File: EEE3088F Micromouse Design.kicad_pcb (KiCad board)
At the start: 2 copper layers, 74.5 x 78.2 mm, 49 parts, among them J1 Conn_02x16_Odd_Even, J2 Conn_01x02, Q2 AO3400A, U1 INA219AxD, U11 DRV8833PW, U12 DRV8833PW, U13 AP22966DC8-7, U15 TP4056-42-ESOP8, U6 TPS5430DDA, U9 CH224K

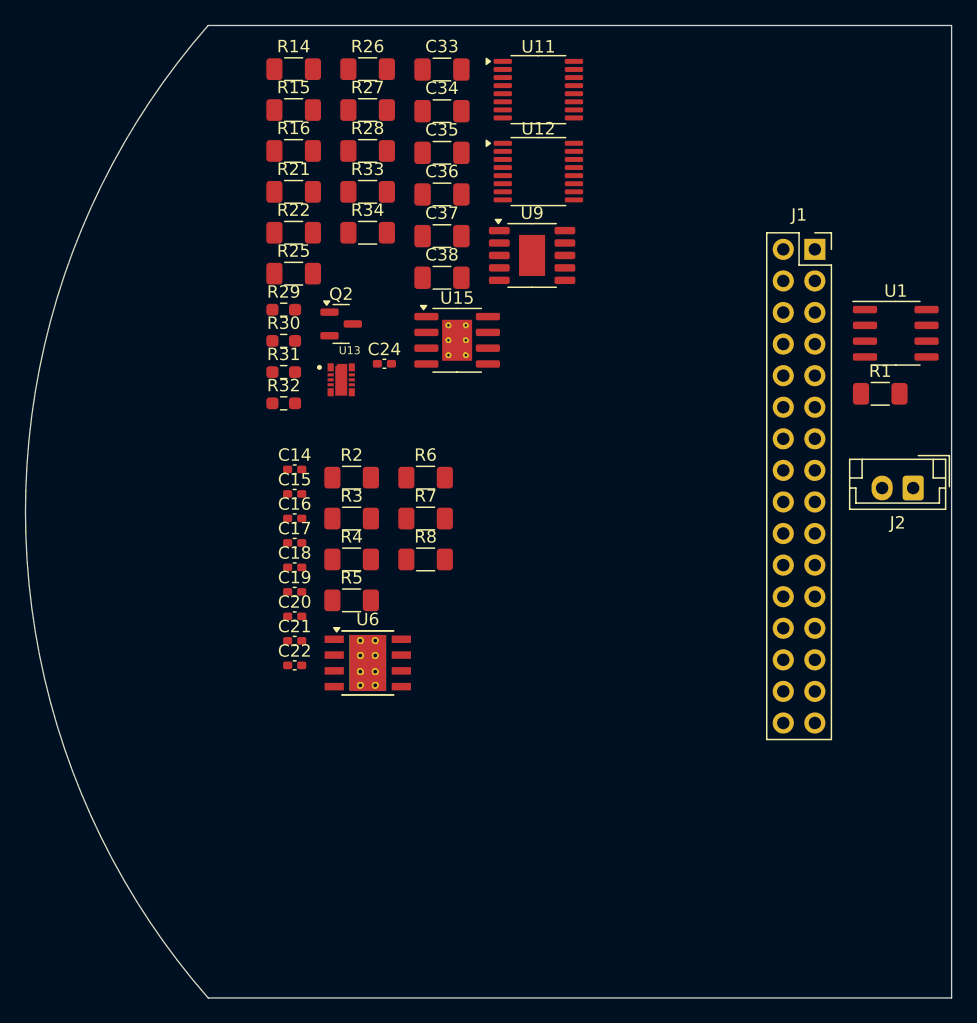
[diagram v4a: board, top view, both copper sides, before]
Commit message: Added footprints for ICs and imported components
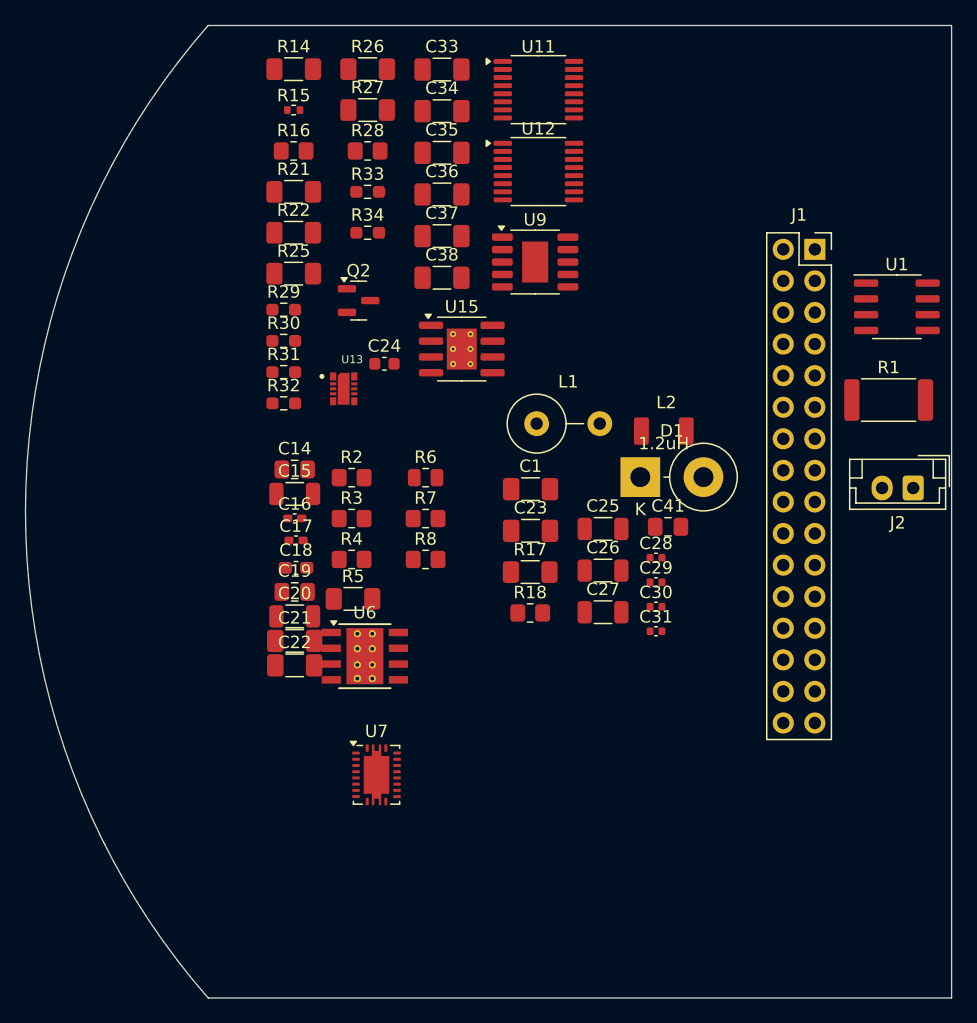
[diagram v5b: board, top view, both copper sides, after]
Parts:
- added C1: 100uF, Capacitor_SMD:C_1206_3216Metric_Pad1.33x1.80mm_HandSolder, F.Cu at (80.4, 94.1)
- added C23: 100uF, Capacitor_SMD:C_1206_3216Metric_Pad1.33x1.80mm_HandSolder, F.Cu at (80.4, 97.4)
- added C25: 10uF, Capacitor_SMD:C_1206_3216Metric, F.Cu at (86.3, 97.3)
- added C26: 10uF, Capacitor_SMD:C_1206_3216Metric, F.Cu at (86.3, 100.6)
- added C27: 10uF, Capacitor_SMD:C_1206_3216Metric, F.Cu at (86.3, 104.0)
- added C28: 2.2uF, Capacitor_SMD:C_0402_1005Metric, F.Cu at (90.5, 99.6)
- added C29: 2.2uF, Capacitor_SMD:C_0402_1005Metric, F.Cu at (90.5, 101.6)
- added C30: 2.2uF, Capacitor_SMD:C_0402_1005Metric, F.Cu at (90.5, 103.5)
- added C31: 2.2uF, Capacitor_SMD:C_0402_1005Metric, F.Cu at (90.5, 105.5)
- added C41: 47uF, Capacitor_SMD:C_0805_2012Metric_Pad1.18x1.45mm_HandSolder, F.Cu at (91.5, 97.1)
- added D1: 1N53xxB, Diode_THT:D_DO-201AD_P5.08mm_Vertical_KathodeUp, F.Cu at (89.3, 93.1)
- added L1: 20uH, Inductor_THT:L_Axial_L11.0mm_D4.5mm_P5.08mm_Vertical_Fastron_MECC, F.Cu at (80.9, 88.8)
- added L2: 1.2uH, Inductor_1.2uH:L_custom_SMD, F.Cu at (91.2, 89.4)
- added R17: 10k, Resistor_SMD:R_1206_3216Metric_Pad1.30x1.75mm_HandSolder, F.Cu at (80.4, 100.7)
- added R18: 10k, Resistor_SMD:R_0805_2012Metric_Pad1.20x1.40mm_HandSolder, F.Cu at (80.4, 104.0)
- added U7: TPS61088RHLR, Package_DFN_QFN:Texas_VQFN-RHL-20, F.Cu at (68.0, 117.0)
- C14: footprint Capacitor_SMD:C_0402_1005Metric_Pad0.74x0.62mm_HandSolder -> Capacitor_SMD:C_0805_2012Metric_Pad1.18x1.45mm_HandSolder
- C15, C20: footprint Capacitor_SMD:C_0402_1005Metric_Pad0.74x0.62mm_HandSolder -> Capacitor_SMD:C_1206_3216Metric
- C18: footprint Capacitor_SMD:C_0402_1005Metric_Pad0.74x0.62mm_HandSolder -> Capacitor_SMD:C_0603_1608Metric_Pad1.08x0.95mm_HandSolder
- C19: value 1.5nF -> 1nF; footprint Capacitor_SMD:C_0402_1005Metric_Pad0.74x0.62mm_HandSolder -> Capacitor_SMD:C_0805_2012Metric_Pad1.18x1.45mm_HandSolder
- C21, C22: footprint Capacitor_SMD:C_0402_1005Metric_Pad0.74x0.62mm_HandSolder -> Capacitor_SMD:C_1206_3216Metric_Pad1.33x1.80mm_HandSolder
- C24: footprint Capacitor_SMD:C_0402_1005Metric_Pad0.74x0.62mm_HandSolder -> Capacitor_SMD:C_0603_1608Metric
- R1: footprint Resistor_SMD:R_1206_3216Metric_Pad1.30x1.75mm_HandSolder -> Resistor_SMD:R_2512_6332Metric
- R15: footprint Resistor_SMD:R_1206_3216Metric_Pad1.30x1.75mm_HandSolder -> Resistor_SMD:R_0402_1005Metric
- R16, R2, R28, R3, R4, R7, R8: footprint Resistor_SMD:R_1206_3216Metric_Pad1.30x1.75mm_HandSolder -> Resistor_SMD:R_0805_2012Metric_Pad1.20x1.40mm_HandSolder
- R33, R34: footprint Resistor_SMD:R_1206_3216Metric_Pad1.30x1.75mm_HandSolder -> Resistor_SMD:R_0603_1608Metric_Pad0.98x0.95mm_HandSolder
- R6: footprint Resistor_SMD:R_1206_3216Metric_Pad1.30x1.75mm_HandSolder -> Resistor_SMD:R_0805_2012Metric
- moved Q2 2.35 mm to (66.6, 78.9)
- moved U1 2.13 mm to (109.9, 79.4)
- moved R1 0.84 mm to (109.2, 86.9)
- moved U15 0.80 mm to (74.9, 82.8)
- moved U13 0.75 mm to (65.4, 86.0)
- moved U6 0.59 mm to (67.1, 107.5)
- moved U9 0.58 mm to (80.8, 75.8)
- moved C17 0.22 mm to (61.6, 98.2)
- moved R5 0.16 mm to (66.2, 102.9)
- moved C18 0.11 mm to (61.6, 100.4)

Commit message: Corrected some footprints and matched LCSC numbers to parts on pcb layout page
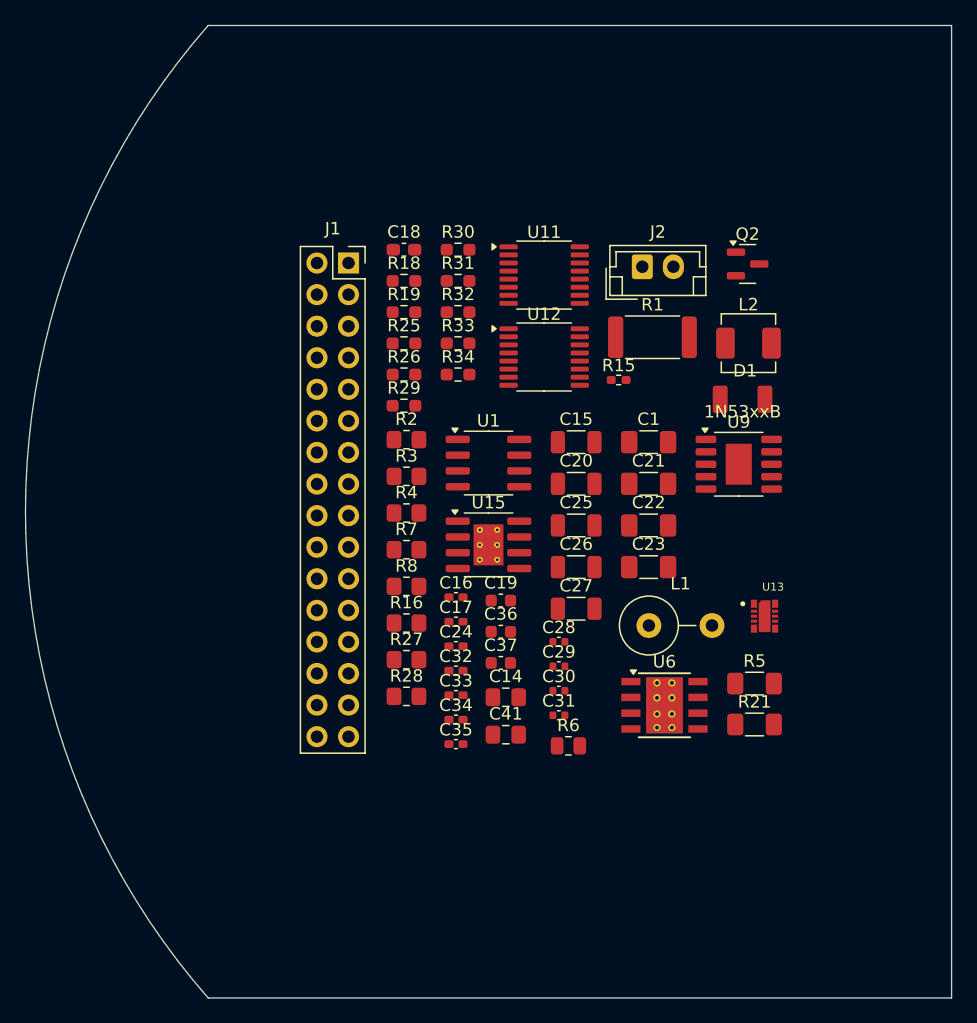
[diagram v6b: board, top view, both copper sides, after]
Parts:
- removed C38: 1nF, Capacitor_SMD:C_1206_3216Metric_Pad1.33x1.80mm_HandSolder
- removed R14, R17, R22: 10k, Resistor_SMD:R_1206_3216Metric_Pad1.30x1.75mm_HandSolder
- removed U7: TPS61088RHLR, Package_DFN_QFN:Texas_VQFN-RHL-20
- added C32: 1uF, Capacitor_SMD:C_0402_1005Metric_Pad0.74x0.62mm_HandSolder, F.Cu at (74.4, 108.7)
- added R19: 10k, Resistor_SMD:R_0603_1608Metric_Pad0.98x0.95mm_HandSolder, F.Cu at (70.2, 79.8)
- C19: footprint Capacitor_SMD:C_0805_2012Metric_Pad1.18x1.45mm_HandSolder -> Capacitor_SMD:C_0603_1608Metric
- C24: footprint Capacitor_SMD:C_0603_1608Metric -> Capacitor_SMD:C_0402_1005Metric_Pad0.74x0.62mm_HandSolder
- C33, C34, C35: value 1μF -> 1uF; footprint Capacitor_SMD:C_1206_3216Metric_Pad1.33x1.80mm_HandSolder -> Capacitor_SMD:C_0402_1005Metric_Pad0.74x0.62mm_HandSolder
- C36: footprint Capacitor_SMD:C_1206_3216Metric_Pad1.33x1.80mm_HandSolder -> Capacitor_SMD:C_0603_1608Metric
- C37: value 1μF -> 1nF; footprint Capacitor_SMD:C_1206_3216Metric_Pad1.33x1.80mm_HandSolder -> Capacitor_SMD:C_0603_1608Metric
- D1: footprint Diode_THT:D_DO-201AD_P5.08mm_Vertical_KathodeUp -> Inductor_1.2uH:L_custom_SMD
- L2: footprint Inductor_1.2uH:L_custom_SMD -> Inductor_SMD:L_Changjiang_FXL0420
- R15: footprint Resistor_SMD:R_0402_1005Metric -> Resistor_SMD:R_0402_1005Metric_Pad0.72x0.64mm_HandSolder
- R18: footprint Resistor_SMD:R_0805_2012Metric_Pad1.20x1.40mm_HandSolder -> Resistor_SMD:R_0603_1608Metric_Pad0.98x0.95mm_HandSolder
- R25, R26: footprint Resistor_SMD:R_1206_3216Metric_Pad1.30x1.75mm_HandSolder -> Resistor_SMD:R_0603_1608Metric_Pad0.98x0.95mm_HandSolder
- R27: footprint Resistor_SMD:R_1206_3216Metric_Pad1.30x1.75mm_HandSolder -> Resistor_SMD:R_0805_2012Metric_Pad1.20x1.40mm_HandSolder
- moved R21 56.7 mm to (98.5, 113.0)
- moved C33 50.3 mm to (74.4, 110.6)
- moved C34 49.0 mm to (74.4, 112.6)
- moved C35 47.6 mm to (74.4, 114.6)
- moved R27 44.3 mm to (70.5, 107.8)
- moved R28 44.0 mm to (70.5, 110.7)
- moved R16 39.0 mm to (70.5, 104.8)
- moved U13 38.5 mm to (99.3, 104.3)
- moved J1 37.5 mm to (65.8, 75.9)
- moved C36 35.5 mm to (78.0, 105.5)
- moved U1 35.2 mm to (77.0, 92.0)
- moved C37 34.7 mm to (78.0, 108.0)
- moved R15 34.0 mm to (87.5, 85.3)
- moved R5 33.0 mm to (98.5, 109.7)
- moved Q2 31.4 mm to (97.9, 76.0)
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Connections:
- C34 pad 1: /5V Out -> /EXT_LOAD1_OUT
- C35 pad 2: /EXT_LOAD1_OUT -> /EXT_LOAD2_OUT
- C37 pad 1: GND -> Net-(U13-SS2)
- C37 pad 2: /EXT_LOAD2_OUT -> GND
- R28 pad 2: Net-(R28-Pad2) -> GND
- R34 pad 2: Net-(R28-Pad2) -> GND

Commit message: Added more footprints
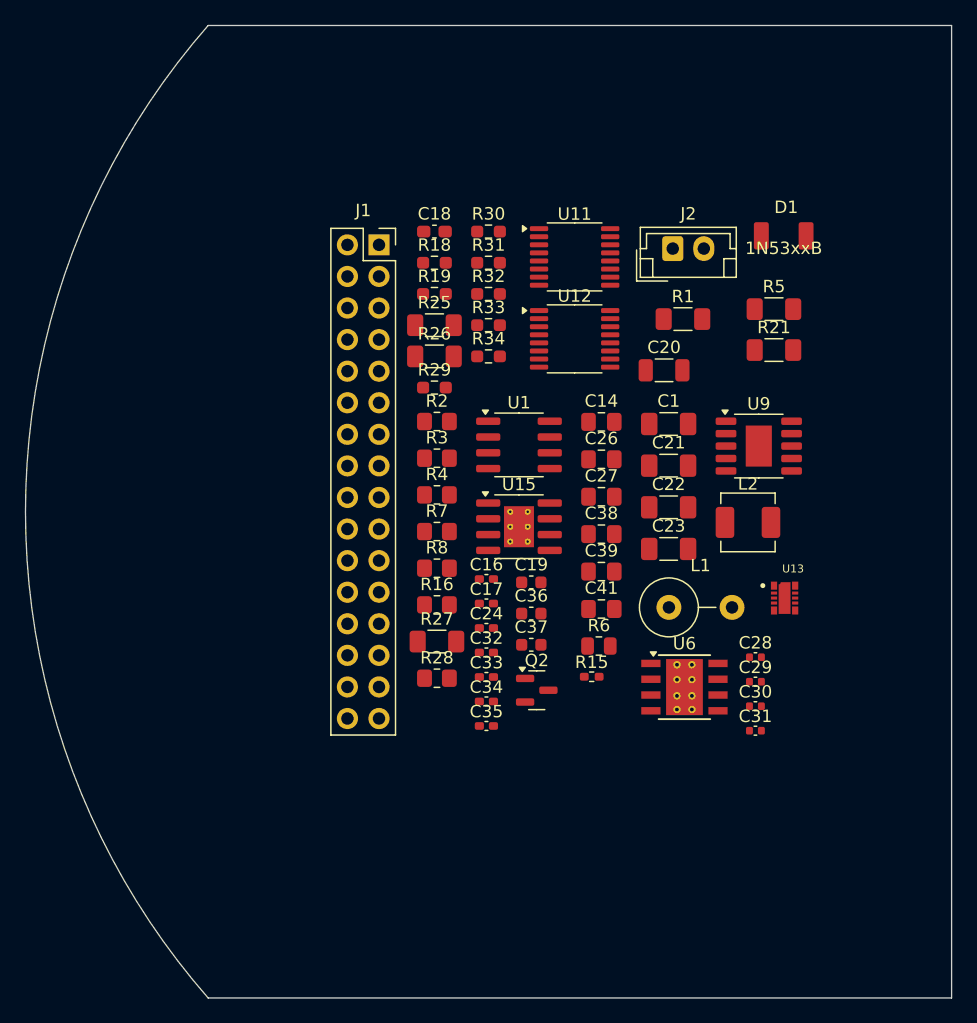
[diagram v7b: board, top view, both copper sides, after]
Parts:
- removed C15, C25: 10uF, Capacitor_SMD:C_1206_3216Metric
- added C38: 10uF, Capacitor_SMD:C_0805_2012Metric_Pad1.18x1.45mm_HandSolder, F.Cu at (86.1, 97.7)
- added C39: 10uF, Capacitor_SMD:C_0805_2012Metric_Pad1.18x1.45mm_HandSolder, F.Cu at (86.1, 100.7)
- C26, C27: footprint Capacitor_SMD:C_1206_3216Metric -> Capacitor_SMD:C_0805_2012Metric_Pad1.18x1.45mm_HandSolder
- R1: footprint Resistor_SMD:R_2512_6332Metric -> Resistor_SMD:R_1206_3216Metric_Pad1.30x1.75mm_HandSolder
- R25, R26: footprint Resistor_SMD:R_0603_1608Metric_Pad0.98x0.95mm_HandSolder -> Resistor_SMD:R_1206_3216Metric_Pad1.30x1.75mm_HandSolder
- R27: footprint Resistor_SMD:R_0805_2012Metric_Pad1.20x1.40mm_HandSolder -> Resistor_SMD:R_1206_3216Metric_Pad1.30x1.75mm_HandSolder
- moved Q2 38.3 mm to (80.9, 110.2)
- moved R21 30.2 mm to (100.0, 82.9)
- moved R5 30.2 mm to (100.0, 79.6)
- moved R15 24.0 mm to (85.3, 109.2)
- moved C14 23.4 mm to (86.1, 88.7)
- moved C28 15.9 mm to (98.5, 107.6)
- moved C29 15.9 mm to (98.5, 109.6)
- moved C30 15.9 mm to (98.5, 111.5)
- moved C31 15.9 mm to (98.5, 113.5)
- moved L2 14.4 mm to (97.9, 96.7)
- moved D1 13.6 mm to (100.8, 73.7)
- moved C41 12.7 mm to (86.1, 103.7)
- moved C20 11.5 mm to (91.2, 84.5)
- moved C27 9.24 mm to (86.1, 94.7)
- moved C26 8.90 mm to (86.1, 91.7)
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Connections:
- U1 pad 5: /V_Battery+ -> /5V Out

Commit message: Added more footprints
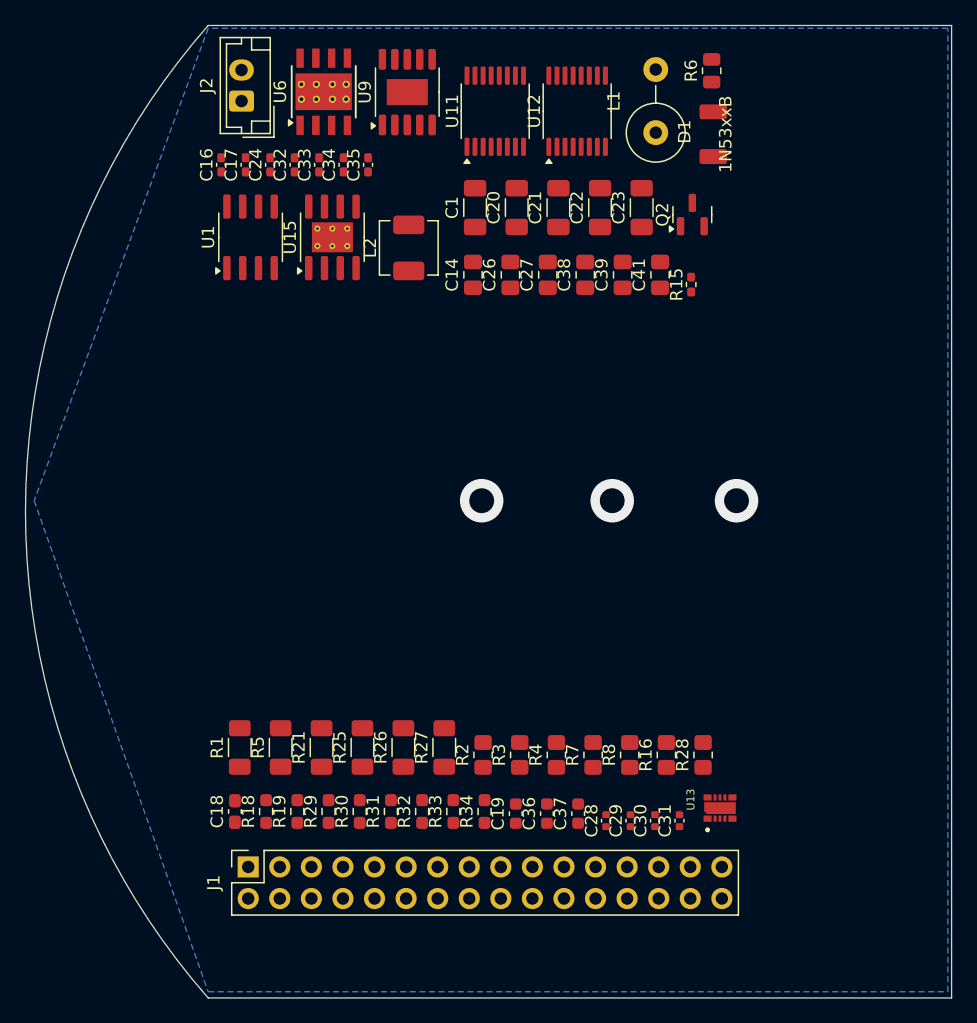
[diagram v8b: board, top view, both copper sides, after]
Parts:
- C20: footprint Capacitor_SMD:C_1206_3216Metric -> Capacitor_SMD:C_1206_3216Metric_Pad1.33x1.80mm_HandSolder
- moved U6 56.0 mm to (63.8, 62.1), turned to 90 degrees
- moved R5 53.1 mm to (60.3, 114.8), turned to 90 degrees
- moved J1 51.1 mm to (57.7, 124.5), turned to 90 degrees
- moved R1 49.6 mm to (57.0, 114.8), turned to 90 degrees
- moved C18 49.3 mm to (56.6, 120.0), turned to 90 degrees
- moved R21 48.4 mm to (63.6, 114.8), turned to 90 degrees
- moved R30 47.8 mm to (66.7, 120.0), turned to 90 degrees
- moved R6 47.2 mm to (95.0, 60.4), turned to 90 degrees
- moved R18 46.2 mm to (59.2, 120.0), turned to 90 degrees
- moved C35 46.1 mm to (67.4, 68.0), turned to 90 degrees
- moved R31 44.8 mm to (69.2, 120.0), turned to 90 degrees
- moved C34 44.7 mm to (65.4, 68.0), turned to 90 degrees
- moved C33 43.3 mm to (63.4, 68.0), turned to 90 degrees
- moved R19 43.1 mm to (61.7, 120.0), turned to 90 degrees
- moved C32 42.2 mm to (61.5, 68.0), turned to 90 degrees
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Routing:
- net GND: vias 0 -> 3
- added copper zone on B.Cu, net GND
